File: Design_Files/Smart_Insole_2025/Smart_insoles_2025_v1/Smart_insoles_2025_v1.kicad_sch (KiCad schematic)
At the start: 14 parts, among them IC1 USBLC6-2SC6, J2 USB_C_Receptacle_USB2.0_16P, SW1 RESET, SW2 BOOT, U5 ESP32-C3-MINI-1-N4

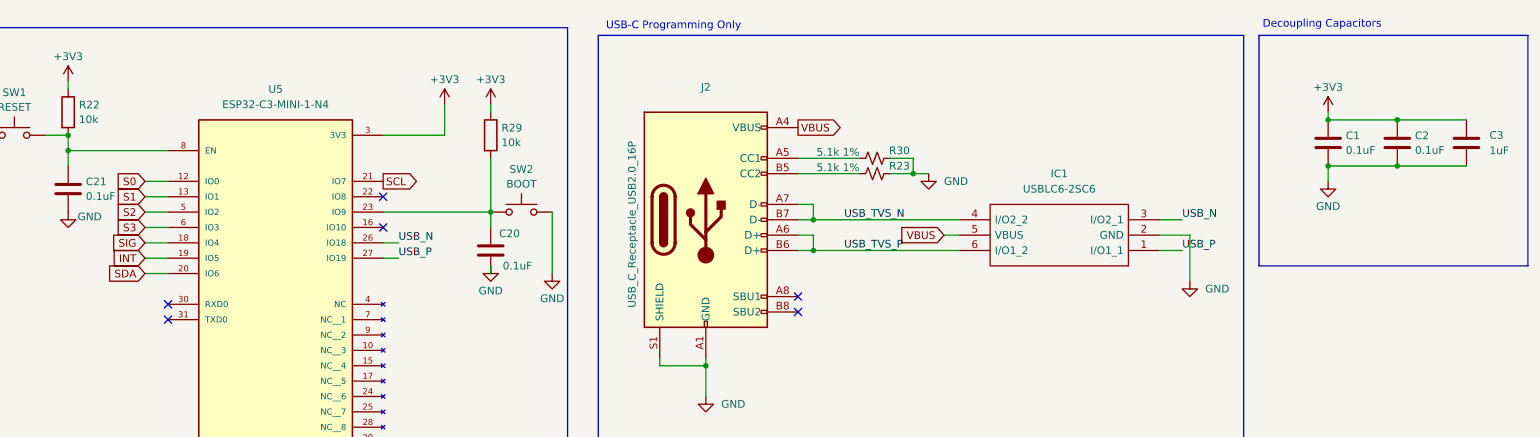
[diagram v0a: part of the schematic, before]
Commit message: SCH: Added test points on idle MCU pins and Power supply. Added ON/OFF switch on VSEL.
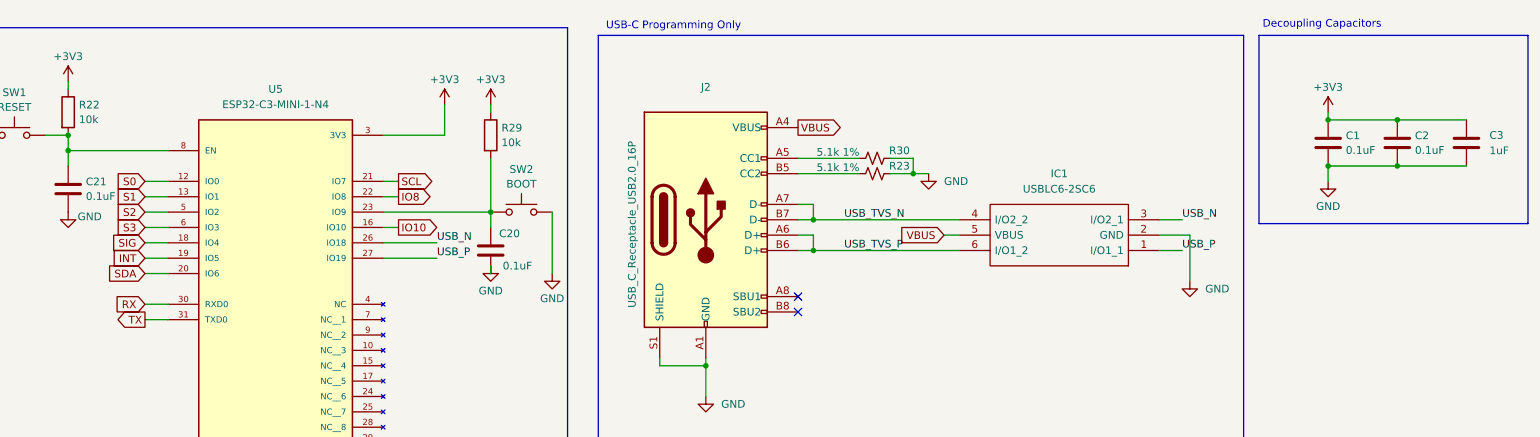
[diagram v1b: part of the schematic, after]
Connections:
- net IO10: now reaches U5.16 (IO10)
- net IO8: now reaches U5.22 (IO8)
- net RX: now reaches U5.30 (RXD0)
- net TX: now reaches U5.31 (TXD0)
- no-connect marks 6 -> 2
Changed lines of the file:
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@@
 	(rectangle
 		(start 234.95 17.78)
-		(end 279.4 55.88)
+		(end 279.4 48.895)
 		(stroke
 			(width 0)
@@
 	)
 	(no_connect
-		(at 90.17 49.53)
-	)
-	(no_connect
 		(at 158.75 60.96)
 	)
-	(no_connect
-		(at 54.61 62.23)
-	)
-	(no_connect
-		(at 90.17 44.45)
-	)
-	(no_connect
-		(at 54.61 64.77)
-	)
 	(wire
 		(pts
@@
 	(wire
 		(pts
+			(xy 92.71 44.45) (xy 90.17 44.45)
+		)
+		(stroke
+			(width 0)
+			(type default)
+		)
+	)
+	(wire
+		(pts
 			(xy 90.17 102.87) (xy 90.17 105.41)
 		)
@@
 	(wire
 		(pts
+			(xy 50.8 64.77) (xy 54.61 64.77)
+		)
+		(stroke
+			(width 0)
+			(type default)
+		)
+	)
+	(wire
+		(pts
 			(xy 161.29 53.34) (xy 161.29 50.8)
 		)
@@
 	(wire
 		(pts
+			(xy 92.71 49.53) (xy 90.17 49.53)
+		)
+		(stroke
+			(width 0)
+			(type default)
+		)
+	)
+	(wire
+		(pts
 			(xy 158.75 50.8) (xy 161.29 50.8)
 		)
@@
 	(wire
 		(pts
+			(xy 92.71 41.91) (xy 90.17 41.91)
+		)
+		(stroke
+			(width 0)
+			(type default)
+		)
+	)
+	(wire
+		(pts
 			(xy 90.17 130.81) (xy 90.17 133.35)
 		)
@@
 	(wire
 		(pts
+			(xy 50.8 62.23) (xy 54.61 62.23)
+		)
+		(stroke
+			(width 0)
+			(type default)
+		)
+	)
+	(wire
+		(pts
 			(xy 21.59 34.29) (xy 24.13 34.29)
 		)
@@
 	(wire
 		(pts
-			(xy 92.71 54.61) (xy 90.17 54.61)
+			(xy 99.06 54.61) (xy 90.17 54.61)
 		)
 		(stroke
@@
 	(wire
 		(pts
-			(xy 92.71 52.07) (xy 90.17 52.07)
+			(xy 99.06 52.07) (xy 90.17 52.07)
 		)
 		(stroke
@@
 	)
 	(label "USB_N"
-		(at 92.71 52.07 0)
+		(at 99.06 52.07 0)
 		(effects
 			(font
@@
 	)
 	(label "USB_P"
-		(at 92.71 54.61 0)
+		(at 99.06 54.61 0)
 		(effects
 			(font
@@
 					(size 1.27 1.27)
 				)
+				(hide yes)
+			)
+		)
+	)
+	(global_label "TX"
+		(shape output)
+		(at 50.8 64.77 180)
+		(fields_autoplaced yes)
+		(effects
+			(font
+				(size 1.27 1.27)
+			)
+			(justify right)
+		)
+		(property "Intersheetrefs" "${INTERSHEET_REFS}"
+			(at 45.6377 64.77 0)
+			(effects
+				(font
+					(size 1.27 1.27)
+				)
+				(justify right)
+				(hide yes)
+			)
+		)
+	)
+	(global_label "IO10"
+		(shape output)
+		(at 92.71 49.53 0)
+		(fields_autoplaced yes)
+		(effects
+			(font
+				(size 1.27 1.27)
+			)
+			(justify left)
+		)
+		(property "Intersheetrefs" "${INTERSHEET_REFS}"
+			(at 100.0495 49.53 0)
+			(effects
+				(font
+					(size 1.27 1.27)
+				)
+				(justify left)
+				(hide yes)
+			)
+		)
+	)
+	(global_label "IO8"
+		(shape output)
+		(at 92.71 44.45 0)
+		(fields_autoplaced yes)
+		(effects
+			(font
+				(size 1.27 1.27)
+			)
+			(justify left)
+		)
+		(property "Intersheetrefs" "${INTERSHEET_REFS}"
+			(at 98.84 44.45 0)
+			(effects
+				(font
+					(size 1.27 1.27)
+				)
+				(justify left)
 				(hide yes)
 			)
@@
 		)
 	)
+	(global_label "RX"
+		(shape input)
+		(at 50.8 62.23 180)
+		(fields_autoplaced yes)
+		(effects
+			(font
+				(size 1.27 1.27)
+			)
+			(justify right)
+		)
+		(property "Intersheetrefs" "${INTERSHEET_REFS}"
+			(at 45.3353 62.23 0)
+			(effects
+				(font
+					(size 1.27 1.27)
+				)
+				(justify right)
+				(hide yes)
+			)
+		)
+	)
 	(global_label "S3"
 		(shape input)
@@
 	(global_label "SCL"
 		(shape output)
-		(at 90.17 41.91 0)
+		(at 92.71 41.91 0)
 		(fields_autoplaced yes)
 		(effects
@@
 		)
 		(property "Intersheetrefs" "${INTERSHEET_REFS}"
-			(at 96.6628 41.91 0)
+			(at 99.2028 41.91 0)
 			(effects
 				(font

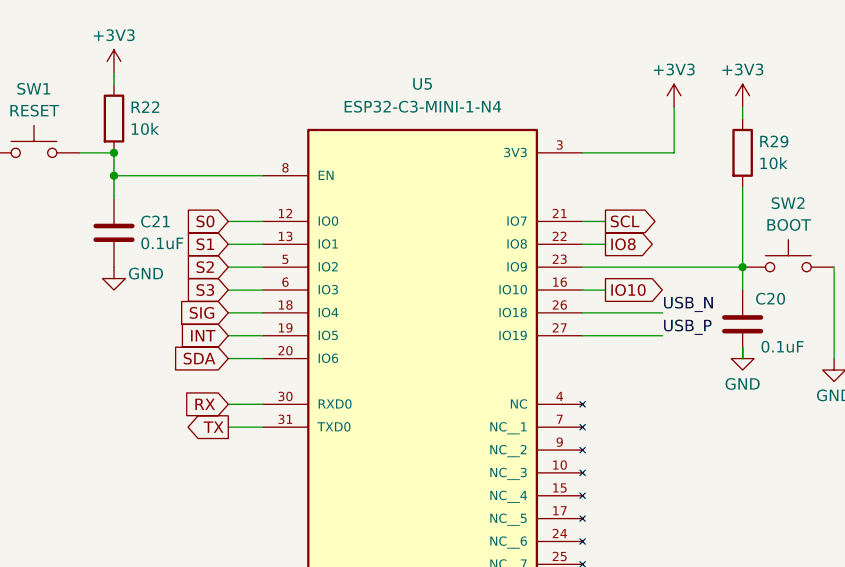
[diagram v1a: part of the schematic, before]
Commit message: PCB: Added 3d models to all components. Also preliminar routing of componentes. Component placemente needs checking.
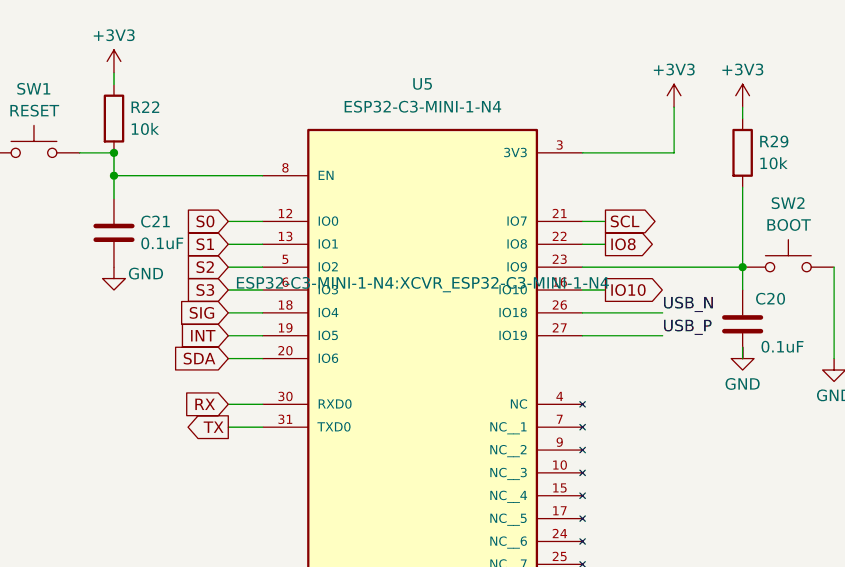
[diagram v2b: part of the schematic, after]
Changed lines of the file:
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@@
 				)
 				(justify bottom)
-				(hide yes)
 			)
 		)
@@
 				(hide yes)
 			)
+		)
+		(property "MPN" ""
+			(at 72.39 49.53 0)
+			(effects
+				(font
+					(size 1.27 1.27)
+				)
+				(hide yes)
+			)
+		)
+		(property "Manufacturer" ""
+			(at 72.39 49.53 0)
+			(effects
+				(font
+					(size 1.27 1.27)
+				)
+				(hide yes)
+			)
+		)
+		(property "3D Model" ""
+			(at 72.39 49.53 0)
+			(effects
+				(font
+					(size 1.27 1.27)
+				)
+				(hide yes)
+			)
+		)
+		(property "Notes" ""
+			(at 72.39 49.53 0)
+			(effects
+				(font
+					(size 1.27 1.27)
+				)
+				(hide yes)
+			)
+		)
+		(property "LCSC Part #" ""
+			(at 72.39 49.53 0)
+			(effects
+				(font
+					(size 1.27 1.27)
+				)
+				(hide yes)
+			)
+		)
+		(property "LCSC MPN" ""
+			(at 72.39 49.53 0)
+			(effects
+				(font
+					(size 1.27 1.27)
+				)
+				(hide yes)
+			)
+		)
+		(property "LCSC MANUFACTURER" ""
+			(at 72.39 49.53 0)
+			(effects
+				(font
+					(size 1.27 1.27)
+				)
+				(hide yes)
+			)
+		)
+		(property "Teste Fabricante" ""
+			(at 72.39 49.53 0)
+			(effects
+				(font
+					(size 1.27 1.27)
+				)
+				(hide yes)
+			)
+		)
+		(property "Teste Numero de parte" ""
+			(at 72.39 49.53 0)
+			(effects
+				(font
+					(size 1.27 1.27)
+				)
+				(hide yes)
+			)

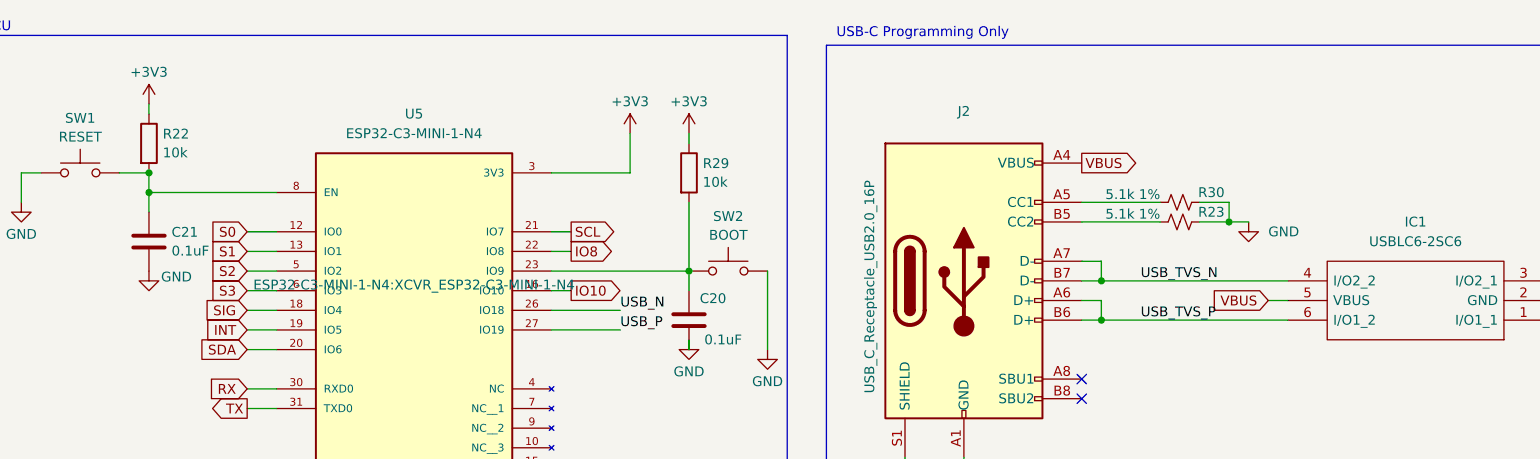
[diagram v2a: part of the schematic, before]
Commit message: PCB:Routing missing connection. Still some missing
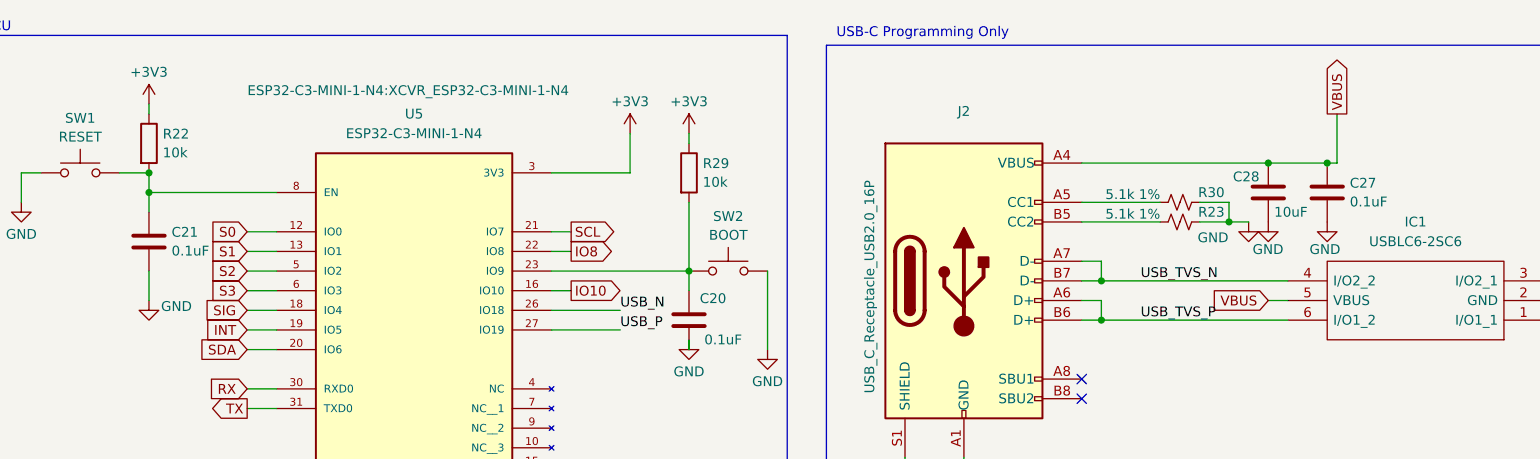
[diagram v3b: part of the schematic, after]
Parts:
- added C27: 0.1uF, Capacitor_SMD:C_0805_2012Metric_Pad1.18x1.45mm_HandSolder, symbol Device:C
- added C28: 10uF, Capacitor_SMD:C_0805_2012Metric_Pad1.18x1.45mm_HandSolder, symbol Device:C
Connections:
- net GND: now also C27.2, C28.2
- net VBUS: now also C27.1, C28.1

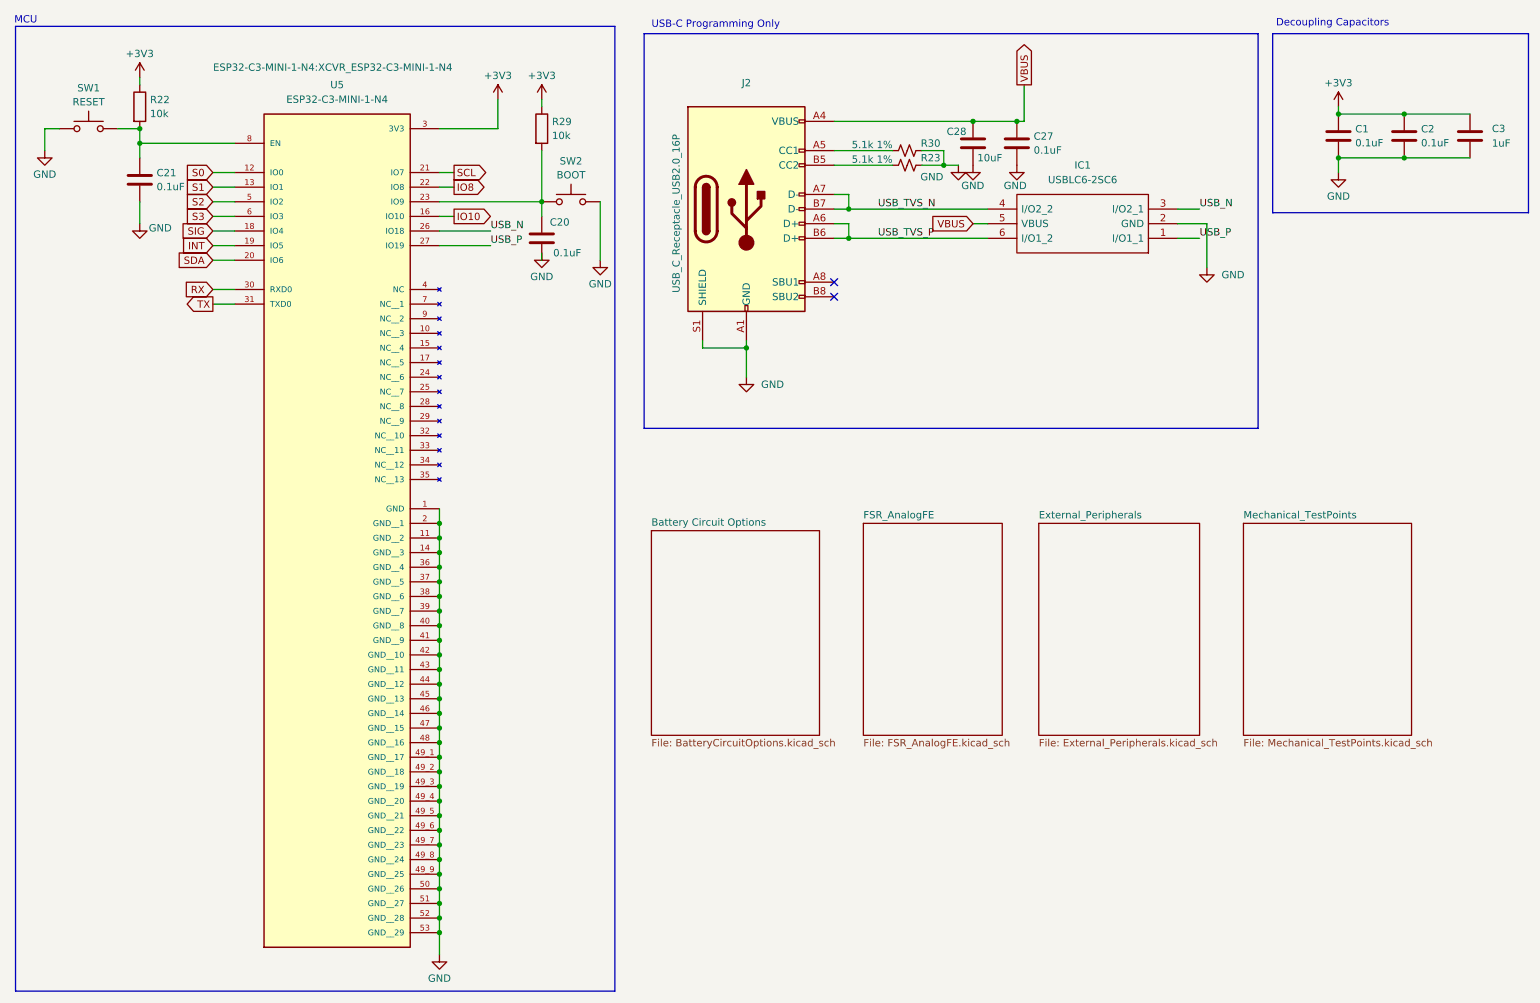
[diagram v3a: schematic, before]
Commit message: SCH:Added pullup resistors on strapping pins.Added 0.1uF on analog input. Added testpoint on missing pad. PCB:Placed new components.Routing refactoring p1
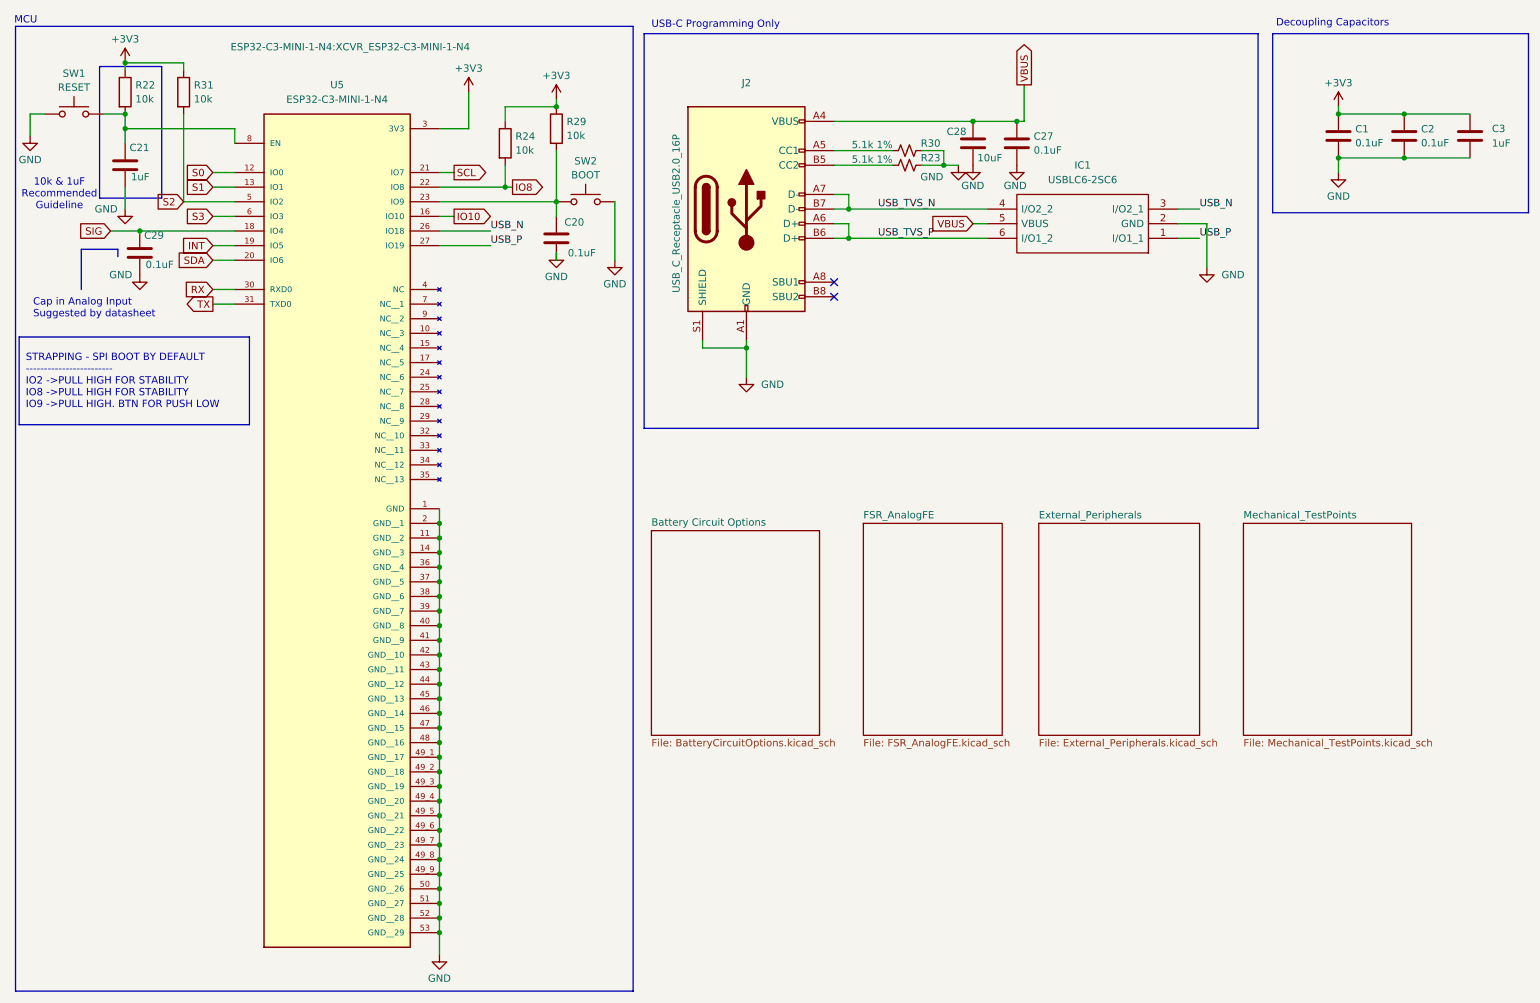
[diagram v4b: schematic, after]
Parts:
- added C29: 0.1uF, Capacitor_SMD:C_0805_2012Metric_Pad1.18x1.45mm_HandSolder, symbol Device:C
- added R24, R31: 10k, Resistor_SMD:R_0805_2012Metric, symbol Device:R
- C21: value 0.1uF -> 1uF
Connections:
- net +3V3: now also R24.1, R31.1
- net GND: now also C29.1
- net IO8: now also R24.2
- net S2: now also R31.2
- net SIG: now also C29.2
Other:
- note added: "10k & 1uF Recommended Guideline"
- note added: "Cap in Analog Input Suggested by datasheet"
- note added: "STRAPPING - SPI BOOT BY DEFAULT ------------------------ IO2 ->PULL HIGH FOR STABILITY IO8 ->PULL HIGH FOR STABILITY IO9 ->PULL HIGH. BTN FOR PUSH LOW"
- moved on the sheet: C20, C21, R22, R29, SW1, SW2

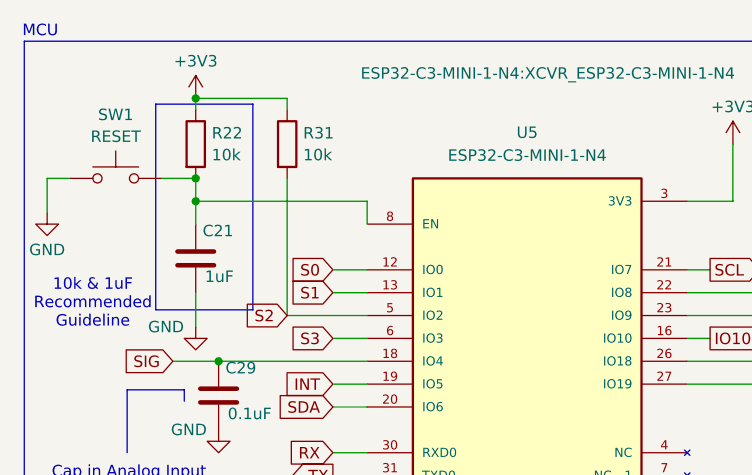
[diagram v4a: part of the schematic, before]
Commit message: PCB:USB Differential pair Impedance calculation and Routing. Also Organized Silkscreen. Added text polarity to battery, boot and rst buttons, and RX TX
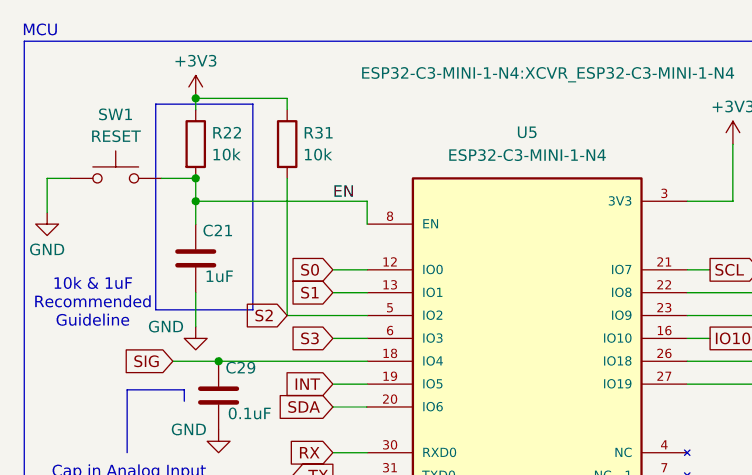
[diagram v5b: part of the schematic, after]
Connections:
- net EN: now reaches C21.2, R22.2, SW1.2, U5.8 (EN)
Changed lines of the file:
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@@
+		)
+	)
+	(label "EN"
+		(at 50.8 34.29 0)
+		(effects
+			(font
+				(size 1.27 1.27)
+			)
+			(justify left bottom)
 		)
 	)

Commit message: PCB:Fixed Multiplexer wrong footprint. Flex Connector modified. Fixed DRC Errors and Warnings
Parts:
- J2: footprint Connector_USB:USB_C_Receptacle_GCT_USB4105-xx-A_16P_TopMnt_Horizontal -> USB_C_Receptacle_16P_SMD_pins_THT_mech:USB_C_Receptacle_GCT_USB4105-xx-A_16P_TopMnt_Horizontal
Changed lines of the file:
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@@
 			)
 		)
-		(property "Footprint" "Connector_USB:USB_C_Receptacle_GCT_USB4105-xx-A_16P_TopMnt_Horizontal"
+		(property "Footprint" "USB_C_Receptacle_16P_SMD_pins_THT_mech:USB_C_Receptacle_GCT_USB4105-xx-A_16P_TopMnt_Horizontal"
 			(at 147.32 48.26 0)
 			(effects
